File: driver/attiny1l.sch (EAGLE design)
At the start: 1 part, among them IC1 TINY13-20SU

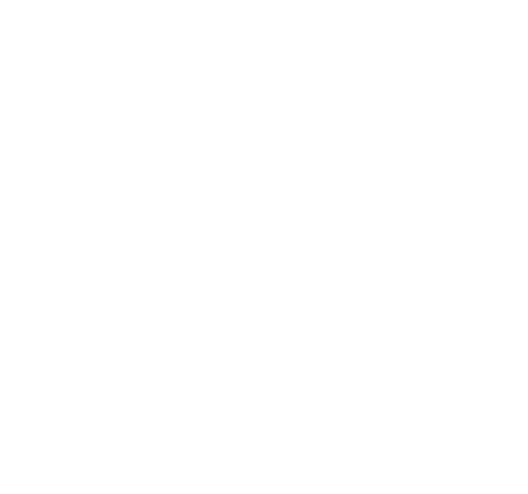
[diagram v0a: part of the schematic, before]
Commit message: gates for splitting the PWM signals so we can live with two PWM outputs instead of 4
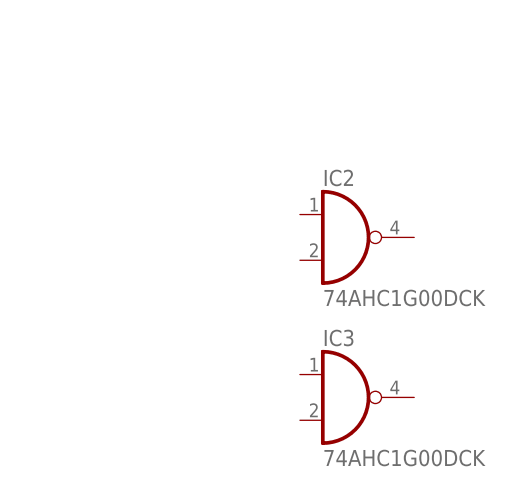
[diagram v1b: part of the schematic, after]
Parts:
- added IC2, IC3: 74AHC1G00DCK, 74xx-little-de:74AHC1G00DCK
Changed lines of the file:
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@@
 <parts>
 <part name="IC1" library="atmel" deviceset="TINY13" device="SU" technology="-20"/>
+<part name="IC2" library="74xx-little-de" deviceset="74*1G00" device="DCK" technology="AHC"/>
+<part name="IC3" library="74xx-little-de" deviceset="74*1G00" device="DCK" technology="AHC"/>
 </parts>
 <sheets>
@@
 <instances>
 <instance part="IC1" gate="G$1" x="30.48" y="78.74" rot="R180"/>
+<instance part="IC2" gate="A" x="91.44" y="55.88"/>
+<instance part="IC3" gate="A" x="91.44" y="38.1"/>
 </instances>
 <busses>

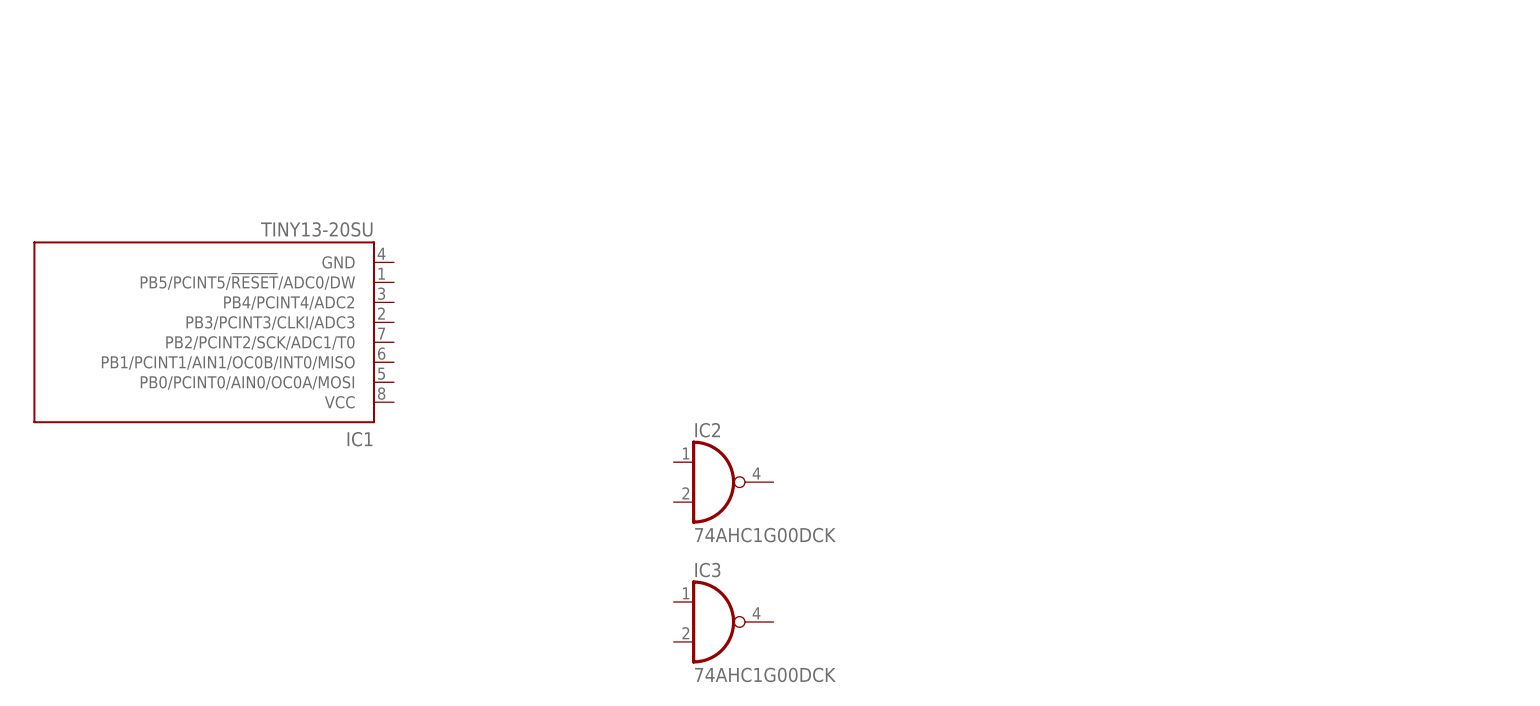
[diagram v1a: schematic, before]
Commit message: made a part for the h-bridge used
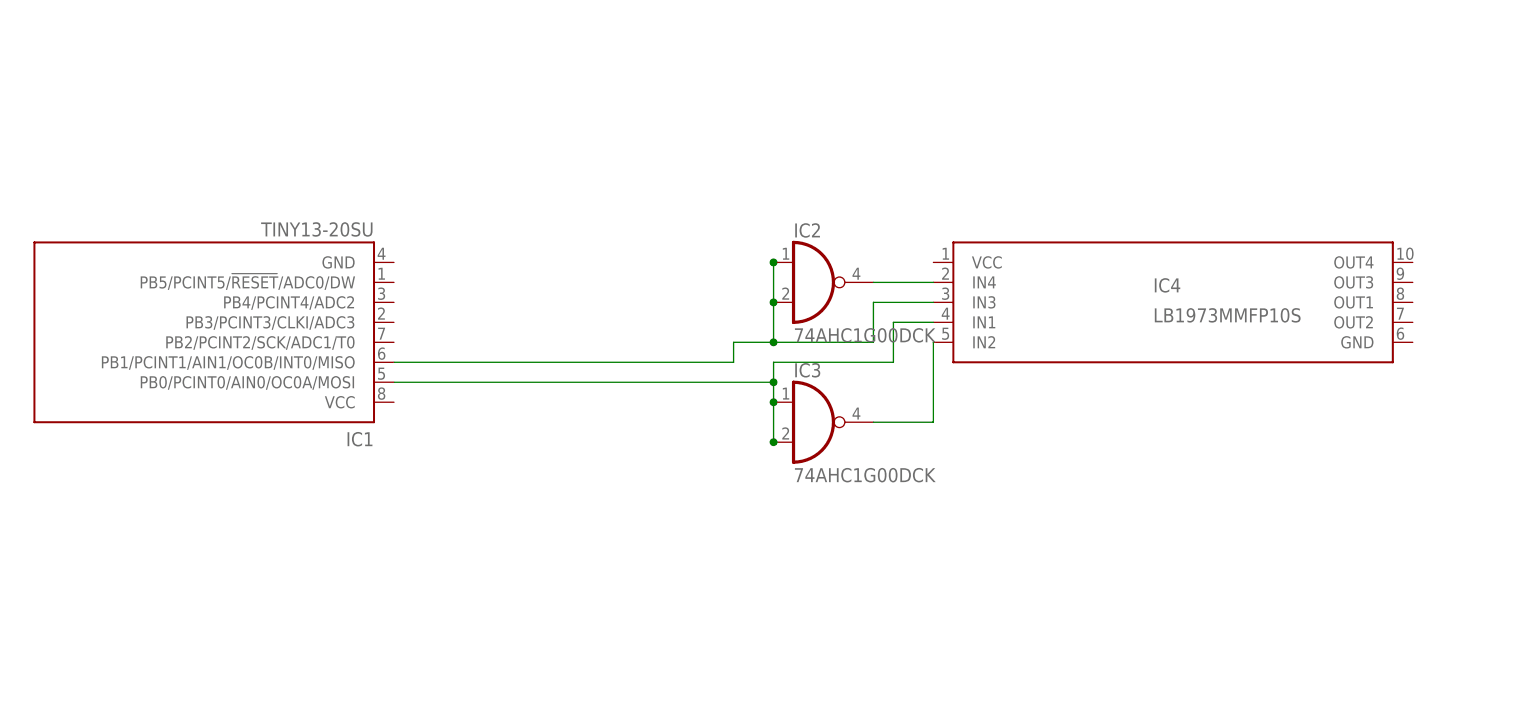
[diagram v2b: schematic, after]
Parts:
- added IC4: LB1973MMFP10S, LB1937M:LB1973MMFP10S
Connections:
- new net N$1: IC3A.O, IC4.IN2
- new net N$2: IC2A.O, IC4.IN4
- new net N$3: IC1.PB0/PCINT0/AIN0/OC0A/MOSI, IC3A.I0, IC3A.I1, IC4.IN1
- new net N$4: IC1.PB1/PCINT1/AIN1/OC0B/INT0/MISO, IC2A.I0, IC2A.I1, IC4.IN3
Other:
- moved on the sheet: IC2, IC3
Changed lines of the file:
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@@
 <?xml version="1.0" encoding="utf-8"?>
 <!DOCTYPE eagle SYSTEM "eagle.dtd">
-<eagle version="6.1">
+<eagle version="6.2">
 <drawing>
 <settings>
@@
 <part name="IC2" library="74xx-little-de" deviceset="74*1G00" device="DCK" technology="AHC"/>
 <part name="IC3" library="74xx-little-de" deviceset="74*1G00" device="DCK" technology="AHC"/>
+<part name="IC4" library="LB1937M" deviceset="LB1973M" device="MFP10S"/>
 </parts>
 <sheets>
@@
 <instances>
 <instance part="IC1" gate="G$1" x="30.48" y="78.74" rot="R180"/>
-<instance part="IC2" gate="A" x="91.44" y="55.88"/>
-<instance part="IC3" gate="A" x="91.44" y="38.1"/>
+<instance part="IC2" gate="A" x="104.14" y="81.28"/>
+<instance part="IC3" gate="A" x="104.14" y="63.5"/>
+<instance part="IC4" gate="G$1" x="149.86" y="78.74"/>
 </instances>
 <busses>
 </busses>
 <nets>
+<net name="N$1" class="0">
+<segment>
+<pinref part="IC3" gate="A" pin="O"/>
+<pinref part="IC4" gate="G$1" pin="IN2"/>
+<wire x1="111.76" y1="63.5" x2="119.38" y2="63.5" width="0.1524" layer="91"/>
+<wire x1="119.38" y1="63.5" x2="119.38" y2="73.66" width="0.1524" layer="91"/>
+</segment>
+</net>
+<net name="N$2" class="0">
+<segment>
+<pinref part="IC2" gate="A" pin="O"/>
+<pinref part="IC4" gate="G$1" pin="IN4"/>
+<wire x1="111.76" y1="81.28" x2="119.38" y2="81.28" width="0.1524" layer="91"/>
+</segment>
+</net>
+<net name="N$3" class="0">
+<segment>
+<pinref part="IC1" gate="G$1" pin="PB0/PCINT0/AIN0/OC0A/MOSI"/>
+<pinref part="IC3" gate="A" pin="I0"/>
+<wire x1="50.8" y1="68.58" x2="99.06" y2="68.58" width="0.1524" layer="91"/>
+<wire x1="99.06" y1="68.58" x2="99.06" y2="66.04" width="0.1524" layer="91"/>
+<pinref part="IC3" gate="A" pin="I1"/>
+<wire x1="99.06" y1="66.04" x2="99.06" y2="60.96" width="0.1524" layer="91"/>
+<wire x1="99.06" y1="68.58" x2="99.06" y2="71.12" width="0.1524" layer="91"/>
+<wire x1="99.06" y1="71.12" x2="114.3" y2="71.12" width="0.1524" layer="91"/>
+<wire x1="114.3" y1="71.12" x2="114.3" y2="76.2" width="0.1524" layer="91"/>
+<pinref part="IC4" gate="G$1" pin="IN1"/>
+<wire x1="114.3" y1="76.2" x2="119.38" y2="76.2" width="0.1524" layer="91"/>
+<junction x="99.06" y="68.58"/>
+<junction x="99.06" y="66.04"/>
+<junction x="99.06" y="60.96"/>
+</segment>
+</net>
+<net name="N$4" class="0">
+<segment>
+<pinref part="IC4" gate="G$1" pin="IN3"/>
+<wire x1="119.38" y1="78.74" x2="111.76" y2="78.74" width="0.1524" layer="91"/>
+<wire x1="111.76" y1="78.74" x2="111.76" y2="73.66" width="0.1524" layer="91"/>
+<pinref part="IC2" gate="A" pin="I1"/>
+<wire x1="111.76" y1="73.66" x2="99.06" y2="73.66" width="0.1524" layer="91"/>
+<wire x1="99.06" y1="73.66" x2="99.06" y2="78.74" width="0.1524" layer="91"/>
+<pinref part="IC2" gate="A" pin="I0"/>
+<wire x1="99.06" y1="78.74" x2="99.06" y2="83.82" width="0.1524" layer="91"/>
+<wire x1="99.06" y1="73.66" x2="93.98" y2="73.66" width="0.1524" layer="91"/>
+<wire x1="93.98" y1="73.66" x2="93.98" y2="71.12" width="0.1524" layer="91"/>
+<pinref part="IC1" gate="G$1" pin="PB1/PCINT1/AIN1/OC0B/INT0/MISO"/>
+<wire x1="93.98" y1="71.12" x2="50.8" y2="71.12" width="0.1524" layer="91"/>
+<junction x="99.06" y="73.66"/>
+<junction x="99.06" y="78.74"/>
+<junction x="99.06" y="83.82"/>
+</segment>
+</net>
 </nets>
 </sheet>

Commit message: the schematic should be ok now, had to sacrificy one HW PWM for the I2C but we should have plenty of cycles to do it in software if neccessary
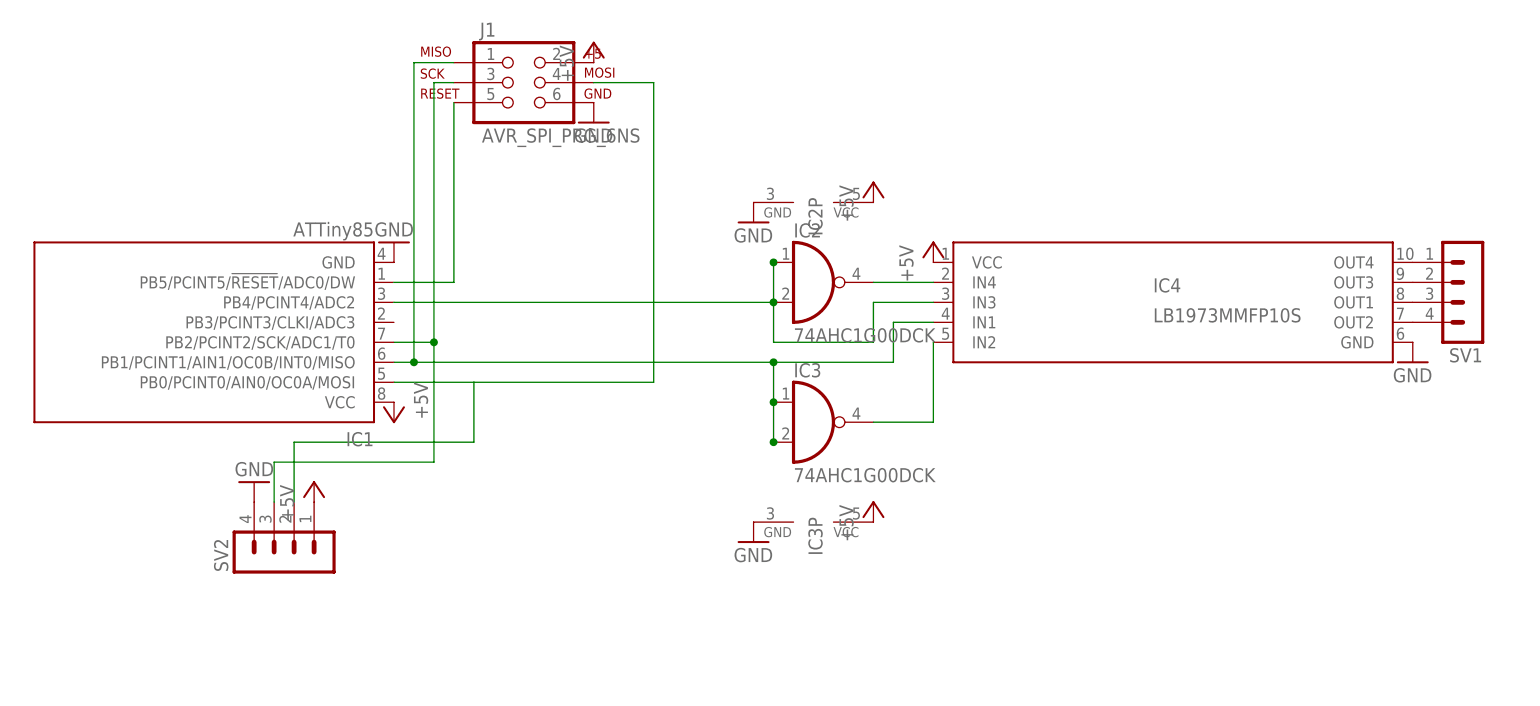
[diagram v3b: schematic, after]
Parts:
- added J1: AVR_SPI_PRG_6NS, SparkFun-Connectors:AVR_SPI_PRG_6NS
- added SV1, SV2: (no value), con-lstb:MA04-1
- IC1: value TINY13-20SU -> ATTiny85
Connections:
- new net +5V: IC1.VCC, IC2P.VCC, IC3P.VCC, IC4.VCC, J1.2, SV2.1
- new net GND: IC1.GND, IC2P.GND, IC3P.GND, IC4.GND, J1.6, SV2.4
- new net N$10: IC4.OUT1, SV1.3
- new net N$11: IC4.OUT2, SV1.4
- new net N$6: IC1.PB5/PCINT5/!RESET!/ADC0/DW, J1.5
- new net N$8: IC4.OUT4, SV1.1
- new net N$9: IC4.OUT3, SV1.2
- new net SCL/SCK: IC1.PB2/PCINT2/SCK/ADC1/T0, J1.3, SV2.3
- new net SDA/MOSI: IC1.PB0/PCINT0/AIN0/OC0A/MOSI, J1.4, SV2.2
- net N$3: now also IC1.PB1/PCINT1/AIN1/OC0B/INT0/MISO, J1.1; no longer IC1.PB0/PCINT0/AIN0/OC0A/MOSI
- net N$4: now also IC1.PB4/PCINT4/ADC2; no longer IC1.PB1/PCINT1/AIN1/OC0B/INT0/MISO

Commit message: very initial placement
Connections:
- net N$1 renamed IN2
- net N$2 renamed IN4
- net N$3 renamed IN1
- net N$4 renamed IN3
- net SCL/SCK: now also SV2.2; no longer SV2.3
- net SDA/MOSI: now also SV2.3; no longer SV2.2
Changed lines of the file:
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@@
 </busses>
 <nets>
-<net name="N$1" class="0">
+<net name="IN2" class="0">
 <segment>
 <pinref part="IC3" gate="A" pin="O"/>
@@
 </segment>
 </net>
-<net name="N$2" class="0">
+<net name="IN4" class="0">
 <segment>
 <pinref part="IC2" gate="A" pin="O"/>
@@
 </segment>
 </net>
-<net name="N$3" class="0">
+<net name="IN1" class="0">
 <segment>
 <pinref part="IC3" gate="A" pin="I0"/>
@@
 </segment>
 </net>
-<net name="N$4" class="0">
+<net name="IN3" class="0">
 <segment>
 <pinref part="IC4" gate="G$1" pin="IN3"/>
@@
 <wire x1="83.82" y1="106.68" x2="76.2" y2="106.68" width="0.1524" layer="91"/>
 <wire x1="60.96" y1="68.58" x2="60.96" y2="60.96" width="0.1524" layer="91"/>
-<pinref part="SV2" gate="1" pin="2"/>
-<wire x1="60.96" y1="60.96" x2="38.1" y2="60.96" width="0.1524" layer="91"/>
-<wire x1="38.1" y1="60.96" x2="38.1" y2="53.34" width="0.1524" layer="91"/>
+<wire x1="60.96" y1="60.96" x2="35.56" y2="60.96" width="0.1524" layer="91"/>
+<pinref part="SV2" gate="1" pin="3"/>
+<wire x1="35.56" y1="60.96" x2="35.56" y2="53.34" width="0.1524" layer="91"/>
 </segment>
 </net>
@@
 <pinref part="J1" gate="G$1" pin="3"/>
 <wire x1="55.88" y1="106.68" x2="58.42" y2="106.68" width="0.1524" layer="91"/>
-<pinref part="SV2" gate="1" pin="3"/>
-<wire x1="35.56" y1="53.34" x2="35.56" y2="58.42" width="0.1524" layer="91"/>
-<wire x1="35.56" y1="58.42" x2="55.88" y2="58.42" width="0.1524" layer="91"/>
+<wire x1="38.1" y1="58.42" x2="55.88" y2="58.42" width="0.1524" layer="91"/>
 <wire x1="55.88" y1="58.42" x2="55.88" y2="73.66" width="0.1524" layer="91"/>
 <junction x="55.88" y="73.66"/>
+<pinref part="SV2" gate="1" pin="2"/>
+<wire x1="38.1" y1="53.34" x2="38.1" y2="58.42" width="0.1524" layer="91"/>
 </segment>
 </net>

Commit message: trying to find got placement
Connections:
- net N$10 renamed OUT1
- net N$11 renamed OUT2
- net N$8 renamed OUT4
- net N$9 renamed OUT3
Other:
- moved on the sheet: SV1
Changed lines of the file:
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@@
 <instance part="GND5" gate="1" x="76.2" y="101.6"/>
 <instance part="P+5" gate="1" x="76.2" y="111.76"/>
-<instance part="SV1" gate="1" x="187.96" y="78.74" rot="R180"/>
+<instance part="SV1" gate="1" x="193.04" y="78.74" rot="R180"/>
 <instance part="SV2" gate="1" x="35.56" y="45.72" rot="R90"/>
 <instance part="P+6" gate="1" x="40.64" y="55.88"/>
@@
 </segment>
 </net>
-<net name="N$8" class="0">
+<net name="OUT4" class="0">
 <segment>
 <pinref part="IC4" gate="G$1" pin="OUT4"/>
 <pinref part="SV1" gate="1" pin="1"/>
+<wire x1="185.42" y1="83.82" x2="180.34" y2="83.82" width="0.1524" layer="91"/>
 </segment>
 </net>
-<net name="N$9" class="0">
+<net name="OUT3" class="0">
 <segment>
 <pinref part="IC4" gate="G$1" pin="OUT3"/>
 <pinref part="SV1" gate="1" pin="2"/>
+<wire x1="185.42" y1="81.28" x2="180.34" y2="81.28" width="0.1524" layer="91"/>
 </segment>
 </net>
-<net name="N$10" class="0">
+<net name="OUT1" class="0">
 <segment>
 <pinref part="IC4" gate="G$1" pin="OUT1"/>
 <pinref part="SV1" gate="1" pin="3"/>
+<wire x1="185.42" y1="78.74" x2="180.34" y2="78.74" width="0.1524" layer="91"/>
 </segment>
 </net>
-<net name="N$11" class="0">
+<net name="OUT2" class="0">
 <segment>
 <pinref part="IC4" gate="G$1" pin="OUT2"/>
 <pinref part="SV1" gate="1" pin="4"/>
+<wire x1="185.42" y1="76.2" x2="180.34" y2="76.2" width="0.1524" layer="91"/>
 </segment>
 </net>

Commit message: it seems the autogenerated package lacked SMD pads in footprint, lets try this again...
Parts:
- removed IC4: LB1973MMFP10S, LB1937M:LB1973MMFP10S
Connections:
- net +5V: no longer IC4.VCC
- net GND: no longer IC4.GND
- net IN1: no longer IC4.IN1
- net IN2: no longer IC4.IN2
- net IN3: no longer IC4.IN3
- net IN4: no longer IC4.IN4
- net OUT1: no longer IC4.OUT1
- net OUT2: no longer IC4.OUT2
- net OUT3: no longer IC4.OUT3
- net OUT4: no longer IC4.OUT4
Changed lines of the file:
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@@
 <part name="IC2" library="74xx-little-de" deviceset="74*1G00" device="DCK" technology="AHC"/>
 <part name="IC3" library="74xx-little-de" deviceset="74*1G00" device="DCK" technology="AHC"/>
-<part name="IC4" library="LB1937M" deviceset="LB1973M" device="MFP10S"/>
 <part name="GND1" library="supply1" deviceset="GND" device=""/>
 <part name="GND2" library="supply1" deviceset="GND" device=""/>
@@
 <instance part="IC2" gate="A" x="104.14" y="81.28"/>
 <instance part="IC3" gate="A" x="104.14" y="63.5"/>
-<instance part="IC4" gate="G$1" x="149.86" y="78.74"/>
 <instance part="IC3" gate="P" x="104.14" y="50.8" rot="R270"/>
 <instance part="IC2" gate="P" x="104.14" y="91.44" rot="R270"/>
@@
 <segment>
 <pinref part="IC3" gate="A" pin="O"/>
-<pinref part="IC4" gate="G$1" pin="IN2"/>
 <wire x1="111.76" y1="63.5" x2="119.38" y2="63.5" width="0.1524" layer="91"/>
 <wire x1="119.38" y1="63.5" x2="119.38" y2="73.66" width="0.1524" layer="91"/>
@@
 <segment>
 <pinref part="IC2" gate="A" pin="O"/>
-<pinref part="IC4" gate="G$1" pin="IN4"/>
 <wire x1="111.76" y1="81.28" x2="119.38" y2="81.28" width="0.1524" layer="91"/>
 </segment>
@@
 <wire x1="99.06" y1="71.12" x2="114.3" y2="71.12" width="0.1524" layer="91"/>
 <wire x1="114.3" y1="71.12" x2="114.3" y2="76.2" width="0.1524" layer="91"/>
-<pinref part="IC4" gate="G$1" pin="IN1"/>
 <wire x1="114.3" y1="76.2" x2="119.38" y2="76.2" width="0.1524" layer="91"/>
 <junction x="99.06" y="66.04"/>
@@
 <net name="IN3" class="0">
 <segment>
-<pinref part="IC4" gate="G$1" pin="IN3"/>
 <wire x1="119.38" y1="78.74" x2="111.76" y2="78.74" width="0.1524" layer="91"/>
 <wire x1="111.76" y1="78.74" x2="111.76" y2="73.66" width="0.1524" layer="91"/>
@@
 </segment>
 <segment>
-<pinref part="IC4" gate="G$1" pin="GND"/>
-<pinref part="GND4" gate="1" pin="GND"/>
-</segment>
-<segment>
 <pinref part="J1" gate="G$1" pin="6"/>
 <pinref part="GND5" gate="1" pin="GND"/>
@@
 </net>
 <net name="+5V" class="0">
-<segment>
-<pinref part="IC4" gate="G$1" pin="VCC"/>
-<pinref part="P+1" gate="1" pin="+5V"/>
-</segment>
 <segment>
 <pinref part="IC2" gate="P" pin="VCC"/>
@@
 <net name="OUT4" class="0">
 <segment>
-<pinref part="IC4" gate="G$1" pin="OUT4"/>
 <pinref part="SV1" gate="1" pin="1"/>
 <wire x1="185.42" y1="83.82" x2="180.34" y2="83.82" width="0.1524" layer="91"/>
@@
 <net name="OUT3" class="0">
 <segment>
-<pinref part="IC4" gate="G$1" pin="OUT3"/>
 <pinref part="SV1" gate="1" pin="2"/>
 <wire x1="185.42" y1="81.28" x2="180.34" y2="81.28" width="0.1524" layer="91"/>
@@
 <net name="OUT1" class="0">
 <segment>
-<pinref part="IC4" gate="G$1" pin="OUT1"/>
 <pinref part="SV1" gate="1" pin="3"/>
 <wire x1="185.42" y1="78.74" x2="180.34" y2="78.74" width="0.1524" layer="91"/>
@@
 <net name="OUT2" class="0">
 <segment>
-<pinref part="IC4" gate="G$1" pin="OUT2"/>
 <pinref part="SV1" gate="1" pin="4"/>
 <wire x1="185.42" y1="76.2" x2="180.34" y2="76.2" width="0.1524" layer="91"/>

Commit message: let us try this again...
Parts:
- added IC4: LB1973M, LB1973M:LB1973M
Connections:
- net +5V: now also IC4.VCC
- net GND: now also IC4.GND
- net IN1: now also IC4.IN1
- net IN2: now also IC4.IN2
- net IN3: now also IC4.IN3
- net IN4: now also IC4.IN4
- net OUT1: now also IC4.OUT1
- net OUT2: now also IC4.OUT2
- net OUT3: now also IC4.OUT2@1
- net OUT4: now also IC4.OUT4
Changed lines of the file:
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@@
 <part name="P+6" library="supply1" deviceset="+5V" device=""/>
 <part name="GND6" library="supply1" deviceset="GND" device=""/>
+<part name="IC4" library="LB1973M" deviceset="LB1973M" device=""/>
 </parts>
 <sheets>
@@
 <instance part="P+6" gate="1" x="40.64" y="55.88"/>
 <instance part="GND6" gate="1" x="33.02" y="55.88" rot="R180"/>
+<instance part="IC4" gate="G$1" x="149.86" y="78.74"/>
 </instances>
 <busses>
@@
 <wire x1="111.76" y1="63.5" x2="119.38" y2="63.5" width="0.1524" layer="91"/>
 <wire x1="119.38" y1="63.5" x2="119.38" y2="73.66" width="0.1524" layer="91"/>
+<pinref part="IC4" gate="G$1" pin="IN2"/>
 </segment>
 </net>
@@
 <pinref part="IC2" gate="A" pin="O"/>
 <wire x1="111.76" y1="81.28" x2="119.38" y2="81.28" width="0.1524" layer="91"/>
+<pinref part="IC4" gate="G$1" pin="IN4"/>
 </segment>
 </net>
@@
 <wire x1="53.34" y1="109.22" x2="53.34" y2="71.12" width="0.1524" layer="91"/>
 <junction x="53.34" y="71.12"/>
+<pinref part="IC4" gate="G$1" pin="IN1"/>
 </segment>
 </net>
@@
 <pinref part="IC1" gate="G$1" pin="PB4/PCINT4/ADC2"/>
 <wire x1="50.8" y1="78.74" x2="99.06" y2="78.74" width="0.1524" layer="91"/>
+<pinref part="IC4" gate="G$1" pin="IN3"/>
 </segment>
 </net>
@@
 <pinref part="GND6" gate="1" pin="GND"/>
 </segment>
+<segment>
+<pinref part="GND4" gate="1" pin="GND"/>
+<pinref part="IC4" gate="G$1" pin="GND"/>
+</segment>
 </net>
 <net name="+5V" class="0">
@@
 <pinref part="SV2" gate="1" pin="1"/>
 <pinref part="P+6" gate="1" pin="+5V"/>
+</segment>
+<segment>
+<pinref part="P+1" gate="1" pin="+5V"/>
+<pinref part="IC4" gate="G$1" pin="VCC"/>
 </segment>
 </net>
@@
 <pinref part="SV1" gate="1" pin="1"/>
 <wire x1="185.42" y1="83.82" x2="180.34" y2="83.82" width="0.1524" layer="91"/>
+<pinref part="IC4" gate="G$1" pin="OUT4"/>
 </segment>
 </net>
@@
 <pinref part="SV1" gate="1" pin="2"/>
 <wire x1="185.42" y1="81.28" x2="180.34" y2="81.28" width="0.1524" layer="91"/>
+<pinref part="IC4" gate="G$1" pin="OUT2@1"/>
 </segment>
 </net>
@@
 <pinref part="SV1" gate="1" pin="3"/>
 <wire x1="185.42" y1="78.74" x2="180.34" y2="78.74" width="0.1524" layer="91"/>
+<pinref part="IC4" gate="G$1" pin="OUT1"/>
 </segment>
 </net>
@@
 <pinref part="SV1" gate="1" pin="4"/>
 <wire x1="185.42" y1="76.2" x2="180.34" y2="76.2" width="0.1524" layer="91"/>
-</segment>
-</net>
+<pinref part="IC4" gate="G$1" pin="OUT2"/>
+</segment>
+</net>

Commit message: 1L routing done, some airwires will be needed but that is to be expected
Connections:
- net IN1 renamed IN1/MISO
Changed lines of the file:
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@@
 </segment>
 </net>
-<net name="IN1" class="0">
+<net name="IN1/MISO" class="0">
 <segment>
 <pinref part="IC3" gate="A" pin="I0"/>
